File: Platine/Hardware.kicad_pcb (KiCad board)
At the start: 2 copper layers, 245 x 250 mm, 174 parts, among them J1 Barrel_Jack_Switch, J2 Screw_Terminal_01x02, J3 USB_B, Q1 BCX19, Q2 BCX19, Q3 DMP3098L7, SW1 SW_Soft_Reset, SW2 SW_Hard_Reset, SW3 SW_Flash, SW4 SW_DPDT_x2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

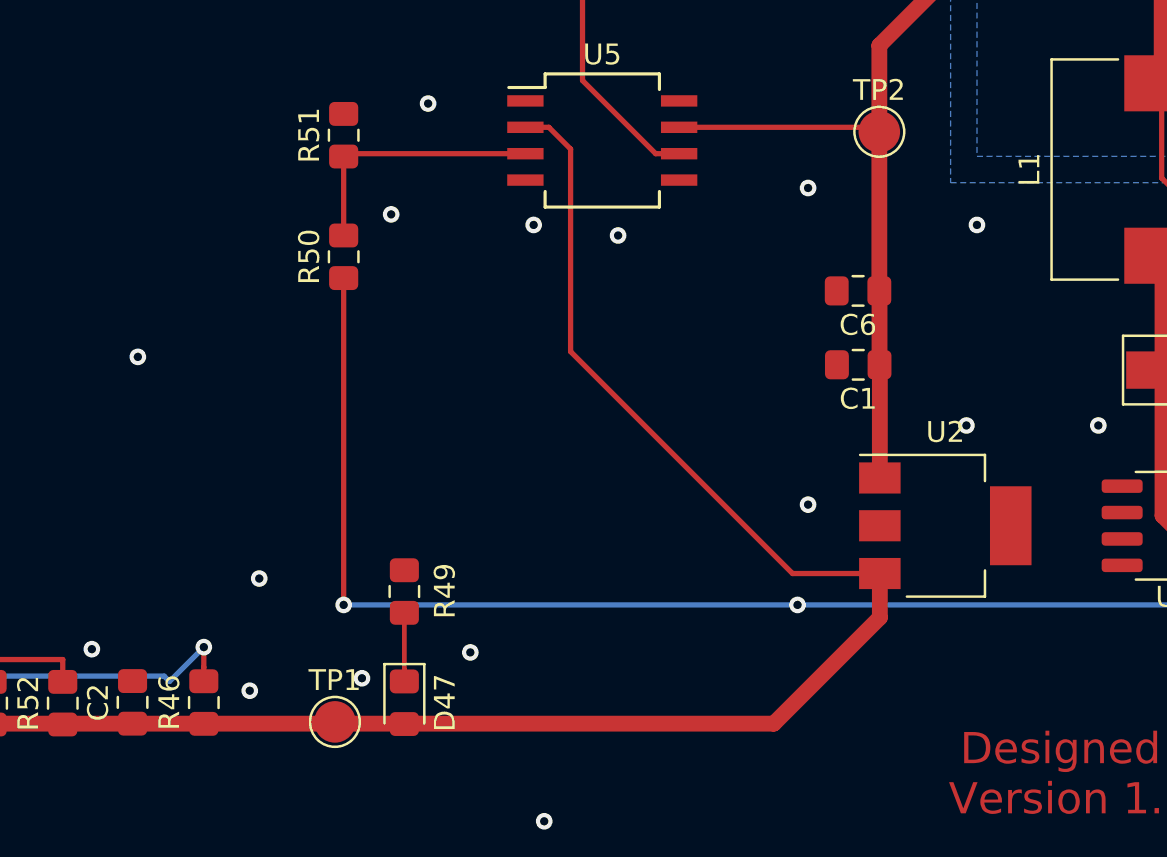
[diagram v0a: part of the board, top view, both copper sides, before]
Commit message: Isolated ZLDO tab from GND Isolated ZLDO 1733 tab from GND (close #2)
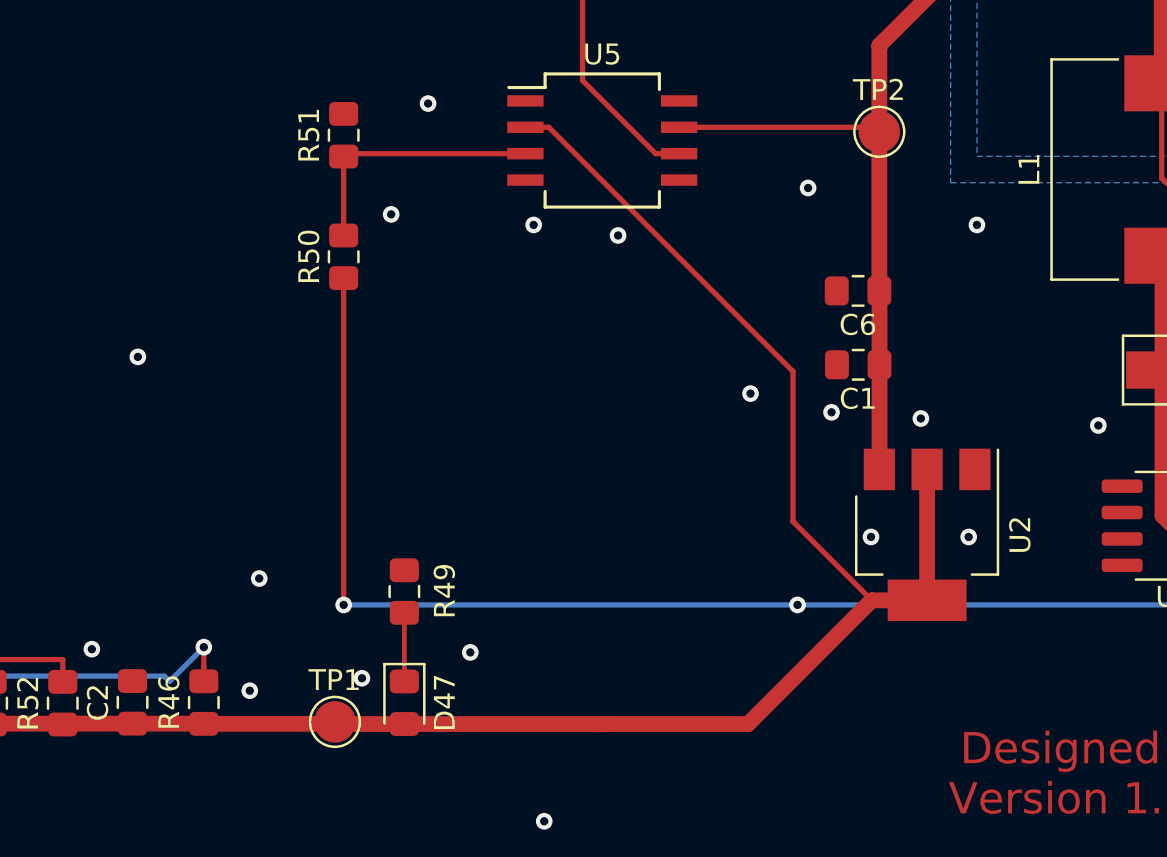
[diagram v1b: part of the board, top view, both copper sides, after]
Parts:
- moved U2 0.98 mm to (200.8, 251.9), turned to 270 degrees
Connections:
- U2 pad 1: VCC -> GND
- U2 pad 2: GND -> VCCQ
- U2 pad 3: VCCQ -> VCC
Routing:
- net VCCQ: track 85.7 -> 91.2 mm
- net GND: vias 70 -> 73
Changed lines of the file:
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@@
     (thickness 1.6)
     (drawings 37)
-    (tracks 914)
+    (tracks 924)
     (zones 0)
     (modules 174)
@@
   )
   (module Package_TO_SOT_SMD:SOT-223-3_TabPin2 (layer F.Cu)
-    (at 201.676 251.46)
+    (at 200.8 251.9 270)
     (descr "module CMS SOT223 4 pins")
     (tags "CMS SOT")
     (attr smd)
-    (fp_text reference U2 (at 0 -4.5) (layer F.SilkS)
+    (fp_text reference U2 (at 0 -4.5 90) (layer F.SilkS)
       (effects (font (size 1 1) (thickness 0.15)))
     )
-    (fp_text value ZLDO1117_SOT223 (at 0 4.5) (layer F.Fab)
+    (fp_text value ZLDO1117_SOT223 (at 0 4.5 90) (layer F.Fab)
       (effects (font (size 1 1) (thickness 0.15)))
     )
@@
     (fp_line (start 1.91 -3.41) (end 1.91 -2.15) (layer F.SilkS) (width 0.12))
     (fp_line (start 1.91 3.41) (end 1.91 2.15) (layer F.SilkS) (width 0.12))
-    (fp_text user %R (at 0 0 -270) (layer F.Fab)
+    (fp_text user %R (at 0 0) (layer F.Fab)
       (effects (font (size 0.8 0.8) (thickness 0.12)))
     )
-    (pad 1 smd rect (at -3.15 -2.3) (size 2 1.5) (layers F.Cu F.Paste F.Mask)
+    (pad 1 smd rect (at -3.15 -2.3 270) (size 2 1.5) (layers F.Cu F.Paste F.Mask)
+      (net 1 GND))
+    (pad 3 smd rect (at -3.15 2.3 270) (size 2 1.5) (layers F.Cu F.Paste F.Mask)
       (net 189 VCC))
-    (pad 3 smd rect (at -3.15 2.3) (size 2 1.5) (layers F.Cu F.Paste F.Mask)
+    (pad 2 smd rect (at -3.15 0 270) (size 2 1.5) (layers F.Cu F.Paste F.Mask)
+      (net 2 VCCQ))
+    (pad 2 smd rect (at 3.15 0 270) (size 2 3.8) (layers F.Cu F.Paste F.Mask)
       (net 2 VCCQ))
-    (pad 2 smd rect (at -3.15 0) (size 2 1.5) (layers F.Cu F.Paste F.Mask)
-      (net 1 GND))
-    (pad 2 smd rect (at 3.15 0) (size 2 3.8) (layers F.Cu F.Paste F.Mask)
-      (net 1 GND))
     (model ${KISYS3DMOD}/Package_TO_SOT_SMD.3dshapes/SOT-223.wrl
       (at (xyz 0 0 0))
@@
   (segment (start 108.541 248.931) (end 106.669 248.931) (width 0.381) (layer F.Cu) (net 1))
   (segment (start 106.669 248.931) (end 106.426 249.174) (width 0.381) (layer F.Cu) (net 1))
-  (via (at 195.072 250.444) (size 0.8) (drill 0.4) (layers F.Cu B.Cu) (net 1))
+  (via (at 198.1 252) (size 0.8) (drill 0.4) (layers F.Cu B.Cu) (net 1))
   (via (at 195.072 235.204) (size 0.8) (drill 0.4) (layers F.Cu B.Cu) (net 1))
   (via (at 185.928 237.49) (size 0.8) (drill 0.4) (layers F.Cu B.Cu) (net 1))
@@
   (via (at 162.814 243.332) (size 0.8) (drill 0.4) (layers F.Cu B.Cu) (net 1))
   (via (at 176.784 231.14) (size 0.8) (drill 0.4) (layers F.Cu B.Cu) (net 1))
-  (via (at 202.692 246.634) (size 0.8) (drill 0.4) (layers F.Cu B.Cu) (net 1))
+  (via (at 200.5 246.3) (size 0.8) (drill 0.4) (layers F.Cu B.Cu) (net 1))
   (via (at 209.042 246.634) (size 0.8) (drill 0.4) (layers F.Cu B.Cu) (net 1))
   (via (at 203.2 236.982) (size 0.8) (drill 0.4) (layers F.Cu B.Cu) (net 1))
@@
   (via (at 160.6 257.4) (size 0.8) (drill 0.4) (layers F.Cu B.Cu) (net 1))
   (via (at 148.9 235) (size 0.8) (drill 0.4) (layers F.Cu B.Cu) (net 1))
-  (segment (start 198.526 255.88) (end 198.526 253.76) (width 0.762) (layer F.Cu) (net 2))
-  (segment (start 162.56 260.985) (end 193.421 260.985) (width 0.762) (layer F.Cu) (net 2))
-  (segment (start 193.421 260.985) (end 198.526 255.88) (width 0.762) (layer F.Cu) (net 2))
+  (via (at 202.8 252) (size 0.8) (drill 0.4) (layers F.Cu B.Cu) (net 1))
+  (via (at 196.2 246) (size 0.8) (drill 0.4) (layers F.Cu B.Cu) (net 1))
+  (via (at 192.3 245.1) (size 0.8) (drill 0.4) (layers F.Cu B.Cu) (net 1))
   (segment (start 162.56 260.985) (end 148.75 260.985) (width 0.762) (layer F.Cu) (net 2))
-  (segment (start 194.324 253.76) (end 198.526 253.76) (width 0.254) (layer F.Cu) (net 2))
-  (segment (start 183.642 243.078) (end 194.324 253.76) (width 0.254) (layer F.Cu) (net 2))
+  (segment (start 165.98 260.985) (end 165.989 260.994) (width 0.762) (layer F.Cu) (net 2))
+  (segment (start 162.56 260.985) (end 165.98 260.985) (width 0.762) (layer F.Cu) (net 2))
+  (segment (start 172.206 260.994) (end 172.3 260.9) (width 0.762) (layer F.Cu) (net 2))
+  (segment (start 165.989 260.994) (end 172.206 260.994) (width 0.762) (layer F.Cu) (net 2))
+  (segment (start 172.403 261.003) (end 172.3 260.9) (width 0.762) (layer F.Cu) (net 2))
+  (segment (start 175.641 261.003) (end 172.403 261.003) (width 0.762) (layer F.Cu) (net 2))
+  (segment (start 175.641 261.003) (end 185.397 261.003) (width 0.762) (layer F.Cu) (net 2))
+  (segment (start 200.8 248.75) (end 200.8 255.05) (width 0.762) (layer F.Cu) (net 2))
+  (segment (start 192.185 261.003) (end 185.397 261.003) (width 0.762) (layer F.Cu) (net 2))
+  (segment (start 198.138 255.05) (end 192.185 261.003) (width 0.762) (layer F.Cu) (net 2))
+  (segment (start 200.8 255.05) (end 198.138 255.05) (width 0.762) (layer F.Cu) (net 2))
+  (segment (start 194.344999 251.256999) (end 198.138 255.05) (width 0.254) (layer F.Cu) (net 2))
+  (segment (start 194.344999 244.032999) (end 194.344999 251.256999) (width 0.254) (layer F.Cu) (net 2))
+  (segment (start 182.595 232.283) (end 194.344999 244.032999) (width 0.254) (layer F.Cu) (net 2))
   (segment (start 181.466 232.283) (end 182.595 232.283) (width 0.254) (layer F.Cu) (net 2))
-  (segment (start 183.642 233.33) (end 183.642 243.078) (width 0.254) (layer F.Cu) (net 2))
-  (segment (start 182.595 232.283) (end 183.642 233.33) (width 0.254) (layer F.Cu) (net 2))
   (segment (start 38.091 204.47) (end 35.061 204.47) (width 0.381) (layer F.Cu) (net 3))
   (segment (start 35.061 200.361) (end 35.05 200.35) (width 0.381) (layer F.Cu) (net 3))
@@
   (segment (start 207.01 221.742) (end 208.026 221.742) (width 0.762) (layer F.Cu) (net 189))
   (segment (start 207.01 221.742) (end 207.01 222.758) (width 0.762) (layer F.Cu) (net 189))
-  (segment (start 198.526 243.729) (end 198.51 243.713) (width 0.762) (layer F.Cu) (net 189))
-  (segment (start 198.526 249.16) (end 198.526 243.729) (width 0.762) (layer F.Cu) (net 189))
   (segment (start 198.51 240.166) (end 198.501 240.157) (width 0.762) (layer F.Cu) (net 189))
   (segment (start 198.51 243.713) (end 198.51 240.166) (width 0.762) (layer F.Cu) (net 189))
@@
   (segment (start 213.5 246.5) (end 214.6 245.4) (width 0.254) (layer F.Cu) (net 189))
   (segment (start 213.5 250.4) (end 213.5 246.5) (width 0.254) (layer F.Cu) (net 189))
+  (segment (start 198.51 248.74) (end 198.5 248.75) (width 0.762) (layer F.Cu) (net 189))
+  (segment (start 198.51 243.713) (end 198.51 248.74) (width 0.762) (layer F.Cu) (net 189))
   (segment (start 250.825 252.73) (end 242.61 252.73) (width 0.762) (layer F.Cu) (net 190))
   (segment (start 242.57 252.69) (end 231.975 252.69) (width 0.762) (layer F.Cu) (net 190))

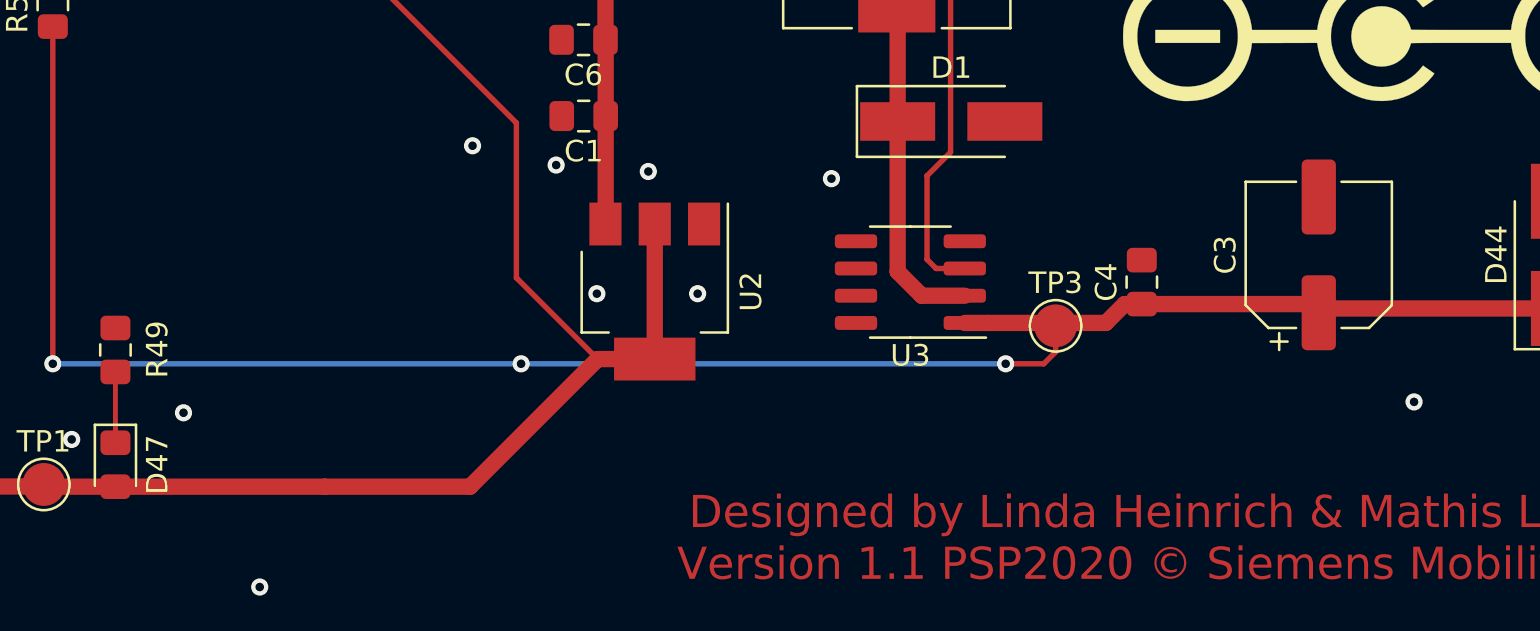
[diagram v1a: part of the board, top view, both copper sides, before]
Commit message: Switched input smoothing cap to 35V rated cap Switched C3 to 35V rated electrolytic capacitor (close #1)
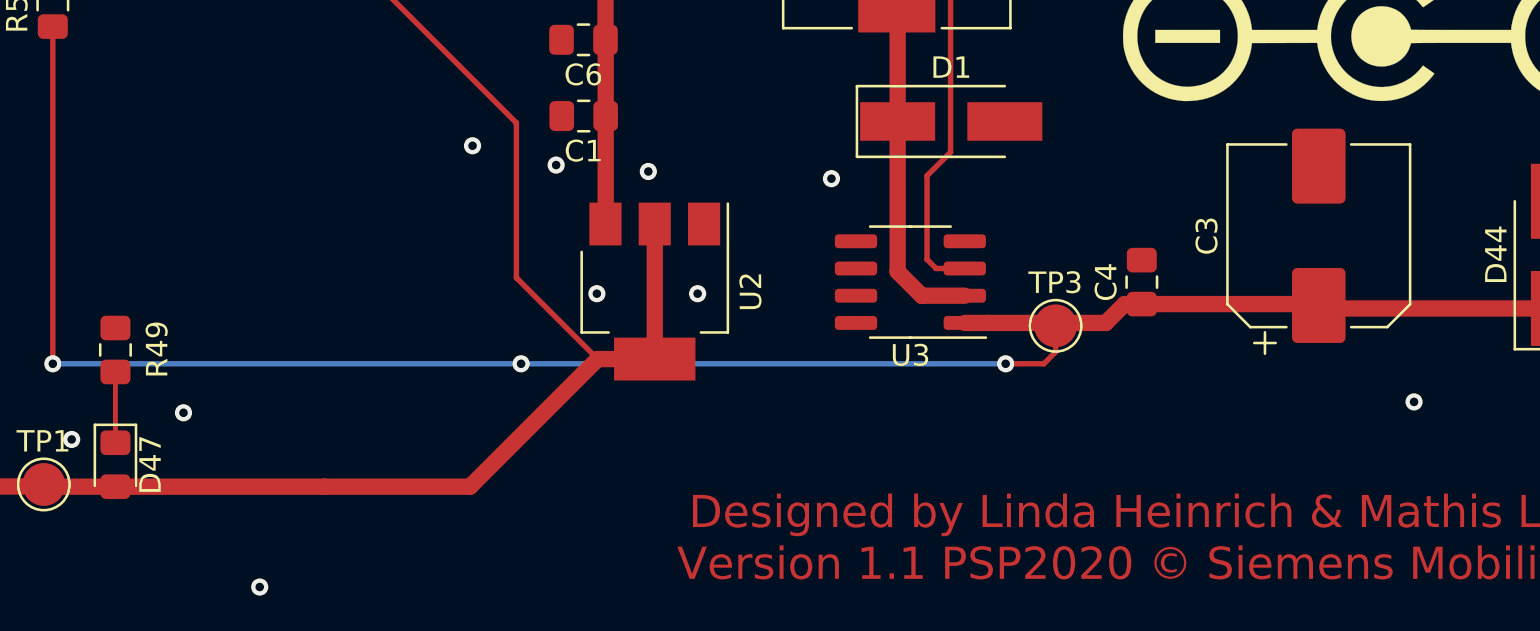
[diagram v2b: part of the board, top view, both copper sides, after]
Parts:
- C3: footprint Capacitor_SMD:CP_Elec_6.3x7.7 -> Capacitor_SMD:CP_Elec_8x10
- D47: footprint Diode_SMD:D_0805_2012Metric_Pad1.15x1.40mm_HandSolder -> LED_SMD:LED_0805_2012Metric_Pad1.15x1.40mm_HandSolder
- moved C3 0.89 mm to (231.8, 249.3)
